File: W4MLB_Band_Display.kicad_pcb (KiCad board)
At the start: 2 copper layers, 72.5 x 68.5 mm, 15 parts, among them J1 SSW-115-01-G-S, J2 SSW-115-01-G-S, J3 SSQ-108-01-T-D-LL, J4 SAMTEC-TST-108-01-X-D, J5 EJ503B, J6 796683-2, J7 PJRAN1X1U01X, J8 PJRAN1X1U01X, J9 Conn_01x10_Pin, U1 ESP32-DEVKIT-V1

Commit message: First release candidate draft
Laid out components and routed signals. Added silkscreen text and artwork
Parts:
- added D3: LED, LED_SMD:LED_0805_2012Metric_Pad1.15x1.40mm_HandSolder, F.Cu at (183.8, 76.5)
- added R1: 330, Resistor_SMD:R_0805_2012Metric_Pad1.20x1.40mm_HandSolder, F.Cu at (179.5, 75.5)
- D1, D2: footprint Diode_THT:D_DO-41_SOD81_P10.16mm_Horizontal -> Diode_SMD:D_0805_2012Metric_Pad1.15x1.40mm_HandSolder
- moved U1 209.4 mm to (37.3, 165.0)
- moved F2 208.1 mm to (17.2, 179.0)
- moved J4 42.9 mm to (162.0, 91.1), turned to 90 degrees
- moved J8 27.7 mm to (141.3, 125.0)
- moved D1 21.8 mm to (142.8, 96.8)
- moved J2 21.8 mm to (147.2, 71.9)
- moved J1 21.8 mm to (121.8, 71.9)
- moved J9 19.6 mm to (125.4, 66.6)
- moved C2 16.0 mm to (174.8, 122.8)
- moved J5 13.9 mm to (182.9, 115.9)
- moved J6 13.8 mm to (181.0, 91.0)
- moved F1 13.5 mm to (182.5, 103.5)
- moved J7 12.5 mm to (126.0, 125.0)
- moved J3 9.22 mm to (134.3, 89.7)
- moved D2 4.94 mm to (150.8, 100.0), turned to -90 degrees
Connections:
- D1 pad 1: GPIO23 -> GPIO17
- D1 pad 2: GPIO22 -> GPIO16
- D2 pad 1: GPIO33 -> GPIO4
- D2 pad 2: GPIO32 -> GPIO15
- J1 pad 08: G1 -> GPIO25
- J1 pad 09: G2 -> GPIO26
- J1 pad 10: E -> GPIO27
- J1 pad 11: B -> GPIO14
- J1 pad 12: D -> GPIO12
- J2 pad 06: B1 -> GPIO19
- J2 pad 08: B2 -> GPIO5
- J2 pad 09: A -> GPIO17
- J2 pad 10: C -> GPIO16
- J2 pad 11: CLK -> GPIO4
- J2 pad 15: +3.3V -> /+3.3VDC
- J3 pad 01: GPIO21 -> GPIO32
- J3 pad 02: G1 -> GPIO23
- J3 pad 03: B1 -> GPIO33
- J3 pad 05: GPIO18 -> GPIO25
- J3 pad 06: G2 -> GPIO22
- J3 pad 07: B2 -> GPIO26
- J3 pad 08: E -> GPIO21
- J3 pad 09: A -> GPIO27
- J3 pad 10: B -> GPIO19
- J3 pad 11: C -> GPIO14
- J3 pad 12: D -> GPIO18
- J3 pad 13: CLK -> GPIO12
- J3 pad 14: GPIO13 -> GPIO5
- J3 pad 15: GPIO15 -> GPIO13
- J4 pad 1: GPIO21 -> GPIO32
- J4 pad 10: B -> GPIO19
- J4 pad 11: C -> GPIO14
- J4 pad 12: D -> GPIO18
- J4 pad 13: CLK -> GPIO12
- J4 pad 14: GPIO13 -> GPIO5
- J4 pad 15: GPIO15 -> GPIO13
- J4 pad 2: G1 -> GPIO23
- J4 pad 3: B1 -> GPIO33
- J4 pad 5: GPIO18 -> GPIO25
- J4 pad 6: G2 -> GPIO22
- J4 pad 7: B2 -> GPIO26
- J4 pad 8: E -> GPIO21
- J4 pad 9: A -> GPIO27
- J7 pad 2: GPIO22 -> GPIO16
- J8 pad 2: GPIO32 -> GPIO15
- J9 pad 1: GPIO39 -> GPIO36
- J9 pad 10: +3.3V -> +5V
- J9 pad 2: GPIO36 -> GPIO39
- J9 pad 3: GPIO35 -> GPIO34
- J9 pad 4: GPIO34 -> GPIO35
- J9 pad 9: +5V -> /+3.3VDC
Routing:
- net +5V: track 0.00 -> 116.7 mm
- net GPIO13: track 0.00 -> 105.7 mm, vias 0 -> 1
- net GPIO12: track 0.00 -> 101.9 mm, vias 0 -> 1
- net GPIO14: track 0.00 -> 96.5 mm, vias 0 -> 1
- net GPIO27: track 0.00 -> 93.5 mm, vias 0 -> 1
- net GPIO26: track 0.00 -> 90.1 mm, vias 0 -> 1
- net GPIO25: track 0.00 -> 87.1 mm, vias 0 -> 1
- net GPIO33: track 0.00 -> 82.6 mm, vias 0 -> 1
- net GPIO32: track 0.00 -> 77.5 mm, vias 0 -> 1
- net GPIO23: track 0.00 -> 53.0 mm
- net /+3.3VDC: track 0.00 -> 50.8 mm, vias 0 -> 1
- net GPIO22: track 1.06 -> 49.7 mm
- net GPIO16: track 0.00 -> 39.8 mm, vias 0 -> 2
- net GPIO2: track 0.00 -> 38.1 mm
- net GPIO21: track 0.00 -> 37.3 mm, vias 0 -> 1
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- added copper zone on F.Cu, net +5V
- added copper zone on F.Cu, net /PWR IN
- added copper zone on B.Cu, net GND
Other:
- board size 72.5 x 68.5 mm -> 71 x 64 mm
- board text added: "* GPIOS 34,35,36,39 INPUT ONLY"
- board text added: "5VDC Power"
- board text added: "GPIO34*"
- board text added: "GPIO35*"
- board text added: "GPIO36*"
- board text added: "GPIO39*"
- board text added: "RXD"
- board text added: "TXD"
- board text removed: "GPIO34/IN ONLY"
- board text removed: "GPIO35/IN ONLY"
- board text removed: "GPIO36/IN ONLY"
- board text removed: "GPIO39/IN ONLY"
- board text removed: "RX"
- board text removed: "TX"

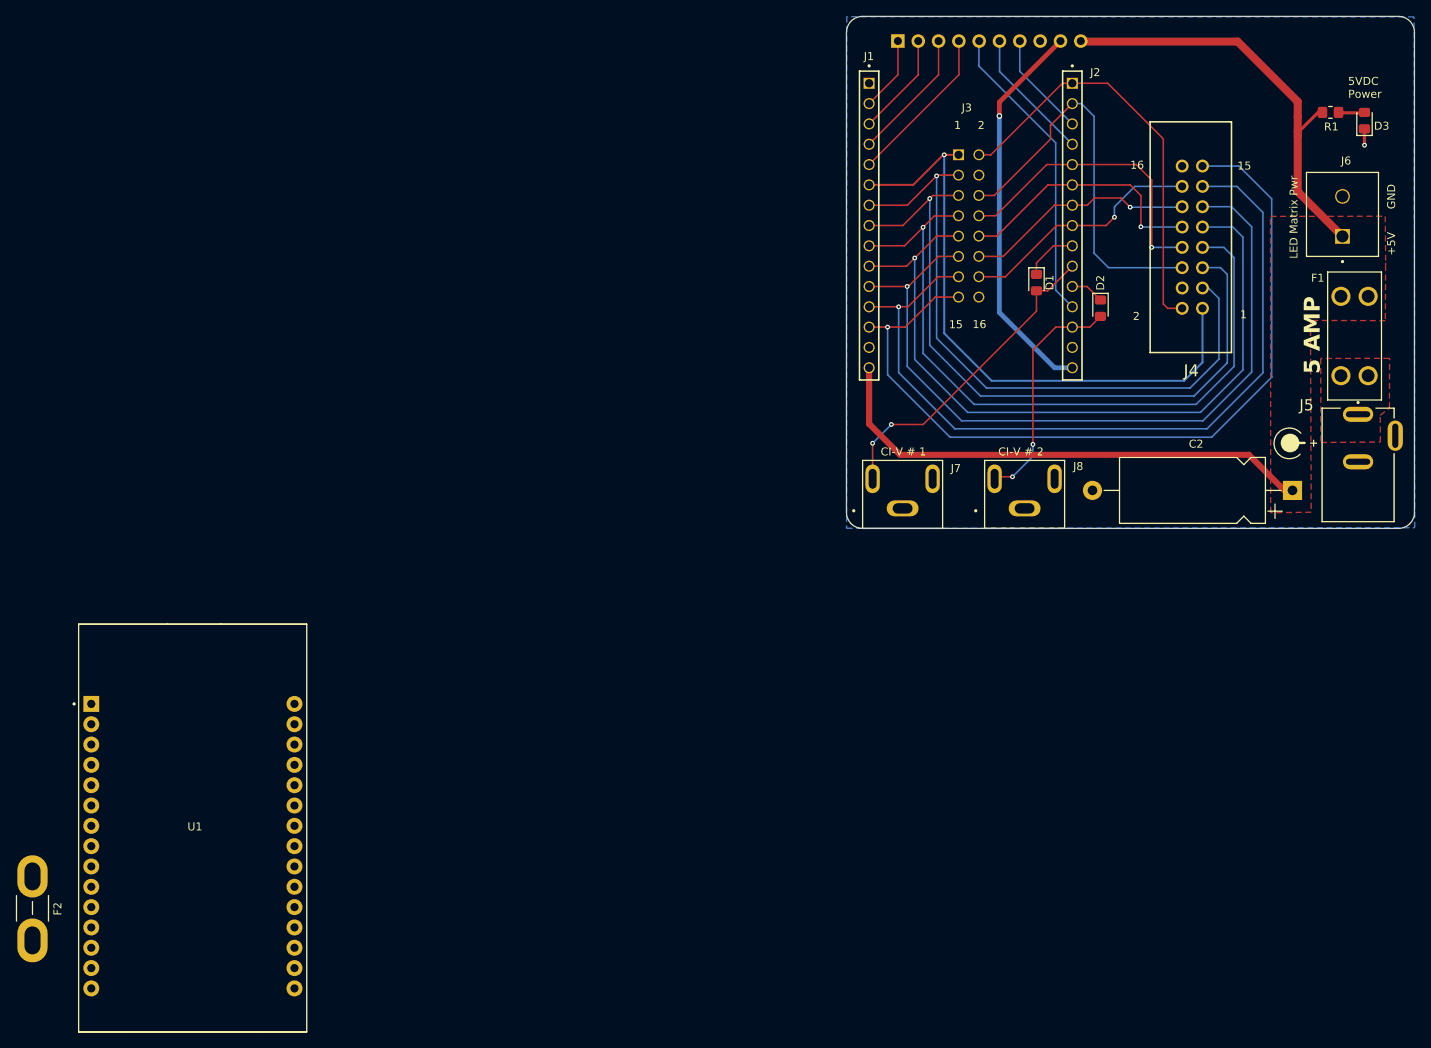
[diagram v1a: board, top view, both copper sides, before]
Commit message: Buzzer
Added buzzer. Rearranged pins to make use of INPUT only pins for RX. Also reallocated different pins to the spare pins header and placed it in a better location.
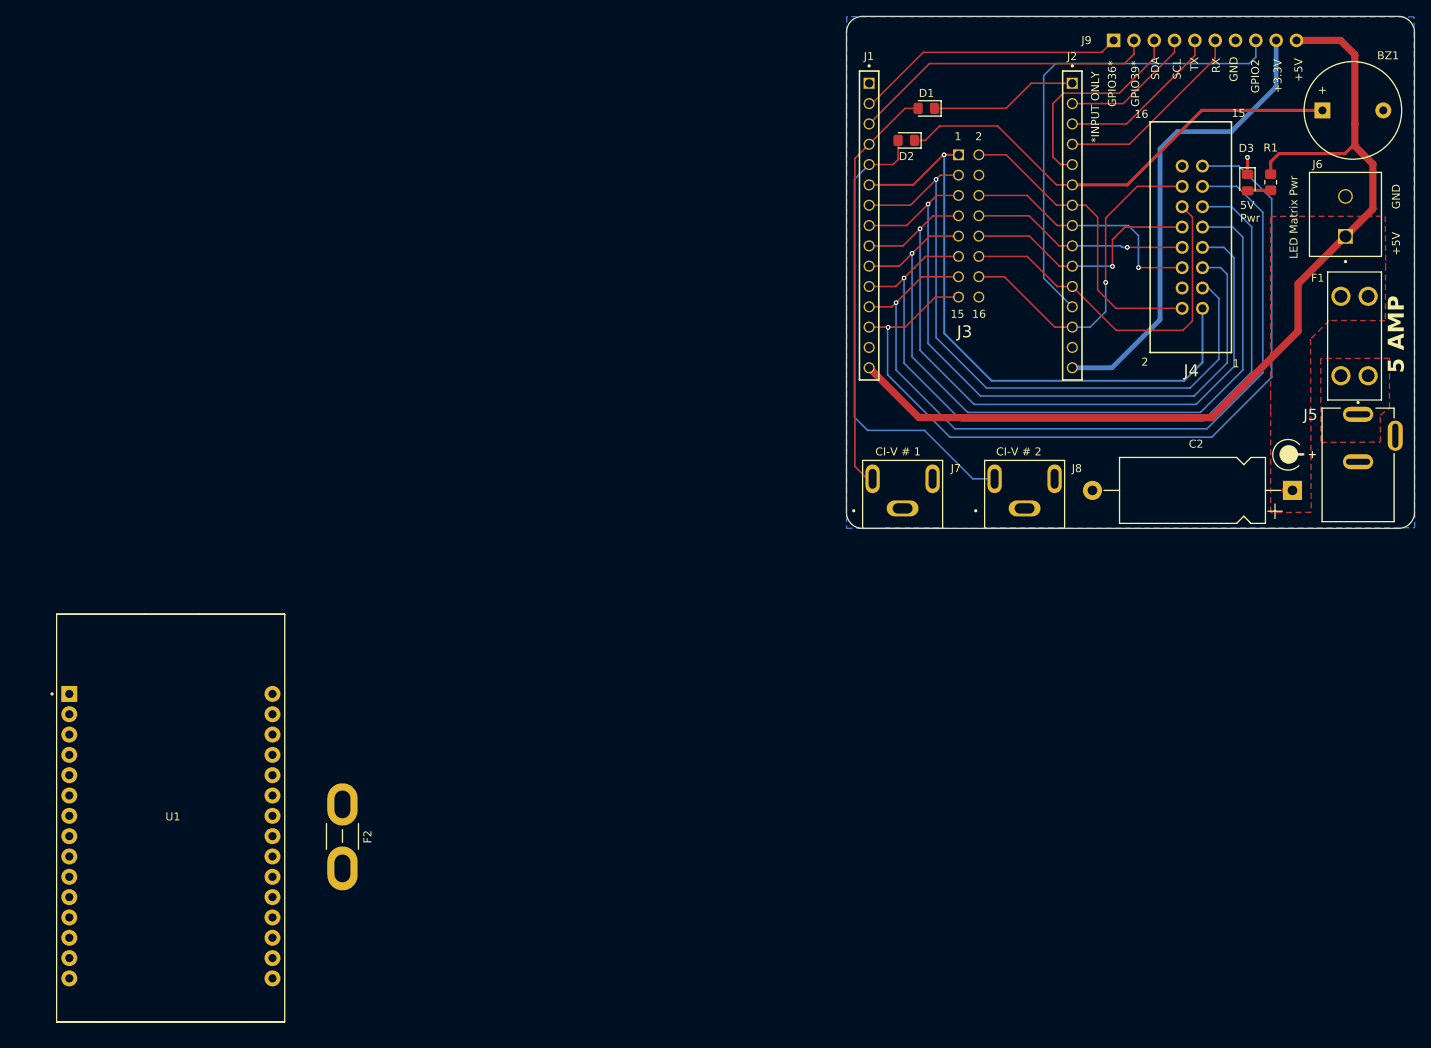
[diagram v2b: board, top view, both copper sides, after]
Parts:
- added BZ1: Buzzer, Buzzer_Beeper:Buzzer_12x9.5RM7.6, F.Cu at (178.5, 75.2)
- moved F2 39.8 mm to (56.0, 170.0)
- moved D2 32.1 mm to (126.5, 79.0), turned to 180 degrees
- moved J9 27.0 mm to (152.4, 66.5)
- moved D1 25.8 mm to (129.0, 75.0), turned to 180 degrees
- moved D3 16.6 mm to (169.1, 84.3), turned to -90 degrees
- moved R1 11.5 mm to (172.0, 84.2), turned to 90 degrees
- moved U1 3.02 mm to (34.5, 163.7)
- moved J6 0.38 mm to (181.4, 91.0)
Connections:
- D1 pad 1: GPIO17 -> GPIO23
- D1 pad 2: GPIO16 -> GPIO34
- D2 pad 1: GPIO4 -> GPIO19
- D2 pad 2: GPIO15 -> GPIO35
- J3 pad 02: GPIO23 -> GPIO18
- J3 pad 06: GPIO22 -> GPIO5
- J3 pad 08: GPIO21 -> GPIO17
- J3 pad 10: GPIO19 -> GPIO16
- J3 pad 12: GPIO18 -> GPIO4
- J3 pad 14: GPIO5 -> GPIO15
- J4 pad 10: GPIO19 -> GPIO16
- J4 pad 12: GPIO18 -> GPIO4
- J4 pad 14: GPIO5 -> GPIO15
- J4 pad 2: GPIO23 -> GPIO18
- J4 pad 6: GPIO22 -> GPIO5
- J4 pad 8: GPIO21 -> GPIO17
- J7 pad 2: GPIO16 -> GPIO34
- J8 pad 2: GPIO15 -> GPIO35
- J9 pad 3: GPIO34 -> GPIO21
- J9 pad 4: GPIO35 -> GPIO22
- J9 pad 5: GPIO2 -> GPIO1
- J9 pad 7: GPIO1 -> GND
- J9 pad 8: GND -> GPIO2
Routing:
- net GPIO4: track 4.22 -> 45.9 mm
- net GPIO35: track 20.1 -> 59.3 mm
- net GPIO34: track 16.5 -> 51.8 mm
- net GPIO23: track 53.0 -> 18.5 mm
- net GPIO22: track 49.7 -> 16.9 mm
- net GPIO19: track 32.5 -> 58.7 mm, vias 1 -> 0
- net GPIO39: track 12.9 -> 38.4 mm
- net GPIO36: track 9.31 -> 33.8 mm
- net GPIO2: track 38.1 -> 59.9 mm
- net GPIO17: track 6.81 -> 27.0 mm, vias 0 -> 1
- net GPIO15: track 29.3 -> 42.2 mm, vias 2 -> 1
- net GPIO21: track 37.3 -> 26.8 mm, vias 1 -> 0
- net GPIO18: track 28.9 -> 38.8 mm, vias 1 -> 0
- net GPIO16: track 39.8 -> 31.0 mm, vias 2 -> 1
- net GPIO3: track 16.7 -> 24.6 mm
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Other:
- board text added: "*INPUT ONLY"
- board text added: "5V Pwr"
- board text added: "RX"
- board text added: "SCL"
- board text added: "SDA"
- board text added: "TX"
- board text removed: "* GPIOS 34,35,36,39 INPUT ONLY"
- board text removed: "5VDC Power"
- board text removed: "GPIO34*"
- board text removed: "GPIO35*"
- board text removed: "RXD"
- board text removed: "TXD"

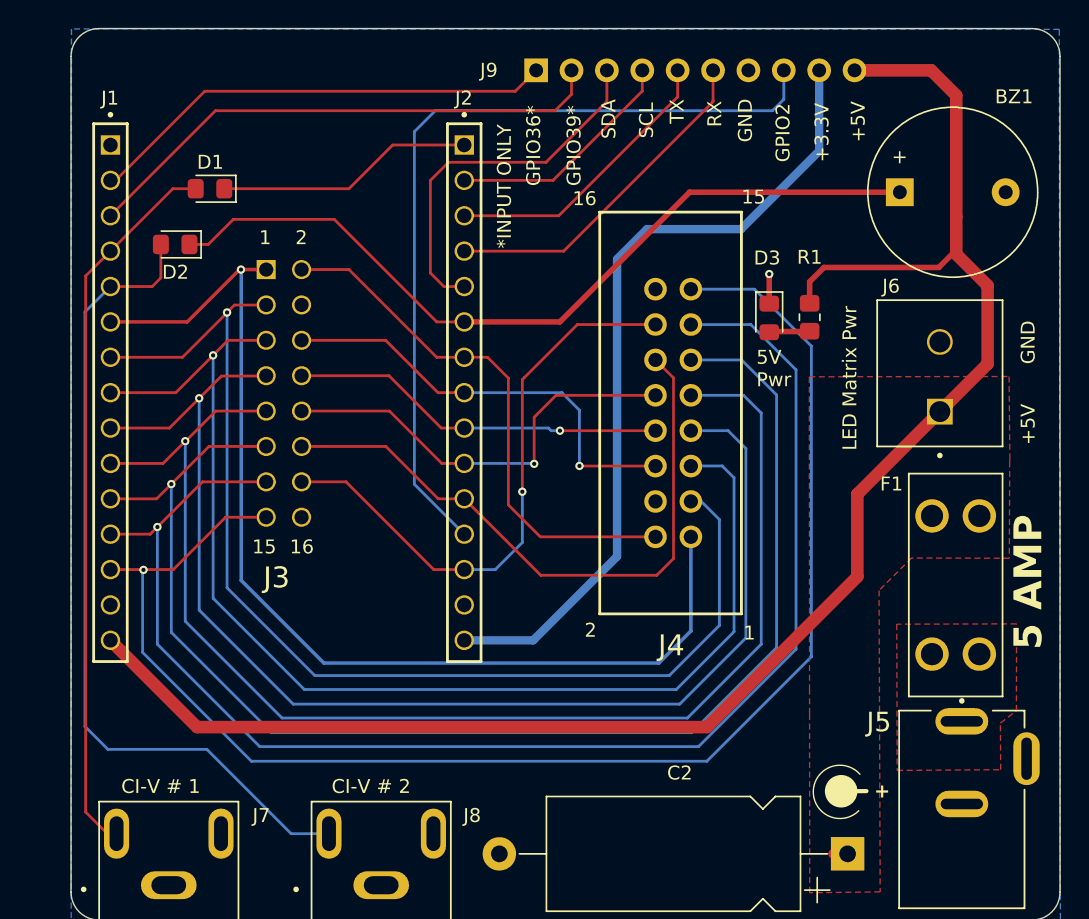
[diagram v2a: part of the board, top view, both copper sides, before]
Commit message: Finisghing touches
Added fillets and chamfers to Cu zones. Adjusted silkscreen text and graphics.
Added mounting holes.
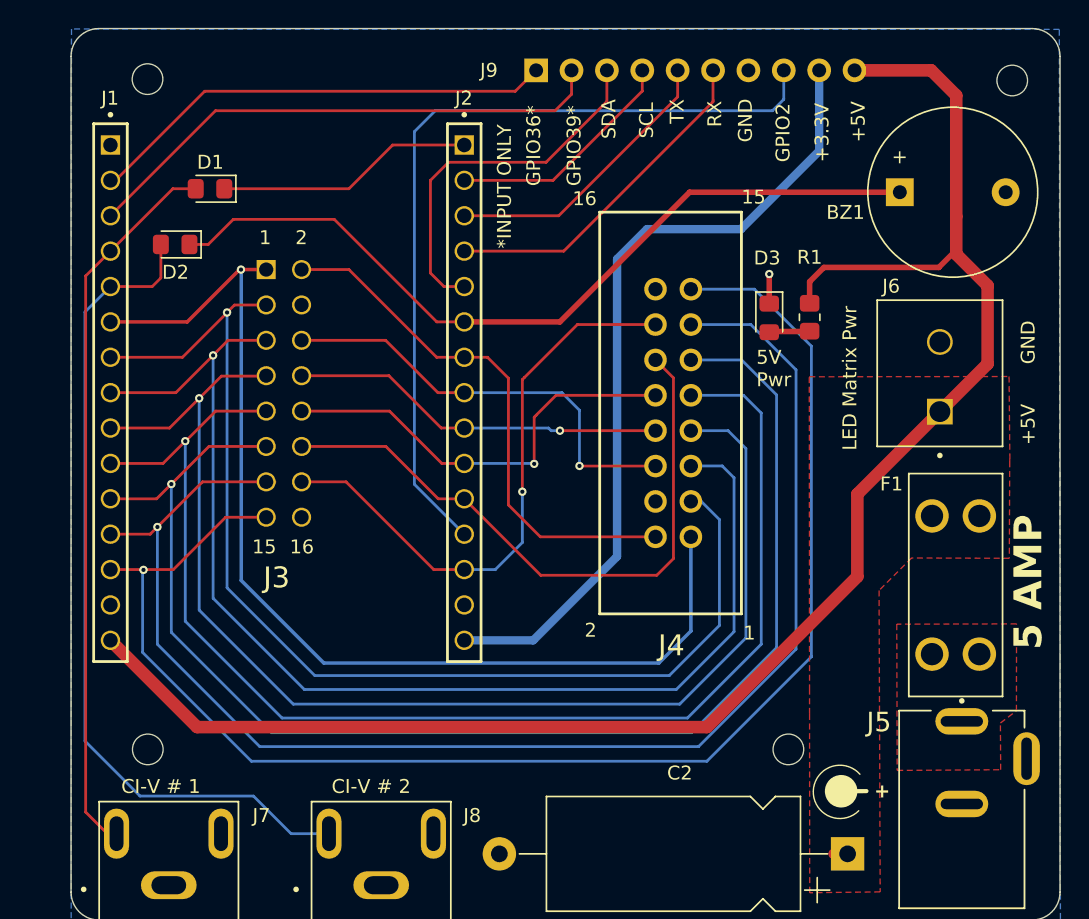
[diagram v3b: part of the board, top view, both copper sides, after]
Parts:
- added REF**: MountingHole_2.2mm_M2, MountingHole:MountingHole_2.2mm_M2, F.Cu at (124.5, 67.1)
- added REF**: MountingHole_2.2mm_M2, MountingHole:MountingHole_2.2mm_M2, F.Cu at (186.6, 67.2)
- added REF**: MountingHole_2.2mm_M2, MountingHole:MountingHole_2.2mm_M2, F.Cu at (124.5, 115.2)
- added REF04: MountingHole_2.2mm_M2, MountingHole:MountingHole_2.2mm_M2, F.Cu at (170.5, 115.2)
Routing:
- net GPIO35: track 59.3 -> 59.9 mm
